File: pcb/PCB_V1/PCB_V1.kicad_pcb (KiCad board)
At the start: 4 copper layers, 100 x 100 mm, 161 parts, among them J201 UART / 3V3 logic, J301 SHT4x / XH 2.50, J302 FLOAT / WAGO 2601, J401 Molex 104031-0811, J501 FAN1 / WAGO 2601, J511 FAN2 / WAGO 2601, J521 PUMP + / switched -, J601 PTC + / switched -, J711 LED1 / large 16S18P panel, J721 LED2 / strip 1, J731 LED3 / strip 2, J901 12 V IN / 25 A design, Q501 AO3400A, Q511 AO3400A, Q521 AO3400A, Q601 NTMFS5C628NLT1G, Q711 100 V N-MOSFET / MPN pending, Q721 100 V N-MOSFET / MPN pending, Q731 100 V N-MOSFET / MPN pending, Q901 P-MOSFET reverse-polarity / M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, SW201 RESET, SW202 BOOT, U101 TPS54202DDCR, U201 ESP32-WROOM-32E-N4, U301 DS3231SN#, U601 UCC27524ADR, U710 LT3756, U720 LT3756, U730 LT3756

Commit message: pcb: repair LED current path and add boost energy storage
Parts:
- added C715: 22u / 25 V X7R / effective >=10u, C_1210_3225Metric, F.Cu at (375.0, 1150.0)
- added C716: 10u / 100 V X7R / effective >=4.7u, C_1210_3225Metric, F.Cu at (175.0, 1200.0)
- added C717: 10u / 100 V X7R / effective >=4.7u, C_1210_3225Metric, F.Cu at (225.0, 1200.0)
- added C725: 22u / 25 V X7R / effective >=10u, C_1210_3225Metric, F.Cu at (225.0, 1250.0)
- added C726: 10u / 100 V X7R / effective >=4.7u, C_1210_3225Metric, F.Cu at (275.0, 1250.0)
- added C727: 10u / 100 V X7R / effective >=4.7u, C_1210_3225Metric, F.Cu at (325.0, 1250.0)
- added C735: 22u / 25 V X7R / effective >=10u, C_1210_3225Metric, F.Cu at (325.0, 1300.0)
- added C736: 10u / 100 V X7R / effective >=4.7u, C_1210_3225Metric, F.Cu at (375.0, 1300.0)
- added C737: 10u / 100 V X7R / effective >=4.7u, C_1210_3225Metric, F.Cu at (175.0, 1350.0)
- C712, C722, C732: value 2.2u / 16 V -> 4.7u / 16 V X7R; footprint C_0603_1608Metric -> C_0805_2012Metric
- R711, R721, R731: value 20k / ~500 kHz preliminary -> 21k / 500 kHz nominal
- R712, R722, R732: value 10k -> 33k / CTRL upper
- R713, R723, R733: value 10k -> 100k / CTRL lower
- R715: value 0.1 / current limit sense -> 0.012 / 1% / >=2W
- R725, R735: value 0.1 / current limit sense -> 0.047 / 1% / >=1W; footprint R_0603_1608Metric -> R_2512_6332Metric
- U710, U720, U730: value LT3756 -> LT3756EMSE-2#PBF
- moved C732 223.6 mm to (175.0, 1300.0)
- moved J711 206.2 mm to (375.0, 1350.0)
- moved L731 206.2 mm to (375.0, 1400.0)
- moved R711 206.2 mm to (375.0, 1450.0)
- moved R716 206.2 mm to (375.0, 1500.0)
- moved R721 206.2 mm to (375.0, 1550.0)
- moved R726 206.2 mm to (375.0, 1600.0)
- moved R731 206.2 mm to (375.0, 1650.0)
- moved R736 206.2 mm to (375.0, 1700.0)
- moved U720 206.2 mm to (375.0, 1750.0)
- moved C722 150.0 mm to (325.0, 1200.0)
- moved C723 150.0 mm to (375.0, 1200.0)
- moved C721 111.8 mm to (275.0, 1200.0)
- moved C724 111.8 mm to (175.0, 1250.0)
- moved D711 111.8 mm to (225.0, 1350.0)
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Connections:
- R716 pad 1: /LEDDrivers/LED1_SENSE_P -> /LEDDrivers/LED1_OUT
- R726 pad 1: /LEDDrivers/LED2_SENSE_P -> /LEDDrivers/LED2_OUT
- R736 pad 1: /LEDDrivers/LED3_SENSE_P -> /LEDDrivers/LED3_OUT
- U710 pad 4: /LEDDrivers/LED1_SENSE_P -> /LEDDrivers/LED1_OUT
- U720 pad 4: /LEDDrivers/LED2_SENSE_P -> /LEDDrivers/LED2_OUT
- U730 pad 4: /LEDDrivers/LED3_SENSE_P -> /LEDDrivers/LED3_OUT

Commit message: pcb: correct power MOSFET pin mapping and reverse input protection
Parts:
- R901: value 100k -> 1M / gate-source
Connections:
- D901 pad 1: +12V_FUSED -> +12V_PROTECTED
- D902 pad 1: +12V_FUSED -> +12V_PROTECTED
- Q711 pad 1: /LEDDrivers/LED1_GATE -> /LEDDrivers/LED1_IS
- Q711 pad 2: /LEDDrivers/LED1_SW -> /LEDDrivers/LED1_IS
- Q711 pad 4: (no net) -> /LEDDrivers/LED1_GATE
- Q711 pad 5: (no net) -> /LEDDrivers/LED1_SW
- Q721 pad 1: /LEDDrivers/LED2_GATE -> /LEDDrivers/LED2_IS
- Q721 pad 2: /LEDDrivers/LED2_SW -> /LEDDrivers/LED2_IS
- Q721 pad 4: (no net) -> /LEDDrivers/LED2_GATE
- Q721 pad 5: (no net) -> /LEDDrivers/LED2_SW
- Q731 pad 1: /LEDDrivers/LED3_GATE -> /LEDDrivers/LED3_IS
- Q731 pad 2: /LEDDrivers/LED3_SW -> /LEDDrivers/LED3_IS
- Q731 pad 4: (no net) -> /LEDDrivers/LED3_GATE
- Q731 pad 5: (no net) -> /LEDDrivers/LED3_SW
- Q901 pad 1: /InputPower/Q901_GATE -> +12V_PROTECTED
- Q901 pad 3: +12V_FUSED -> +12V_PROTECTED
- Q901 pad 4: (no net) -> /InputPower/Q901_GATE
- Q901 pad 5: (no net) -> +12V_FUSED
- R901 pad 1: +12V_FUSED -> +12V_PROTECTED

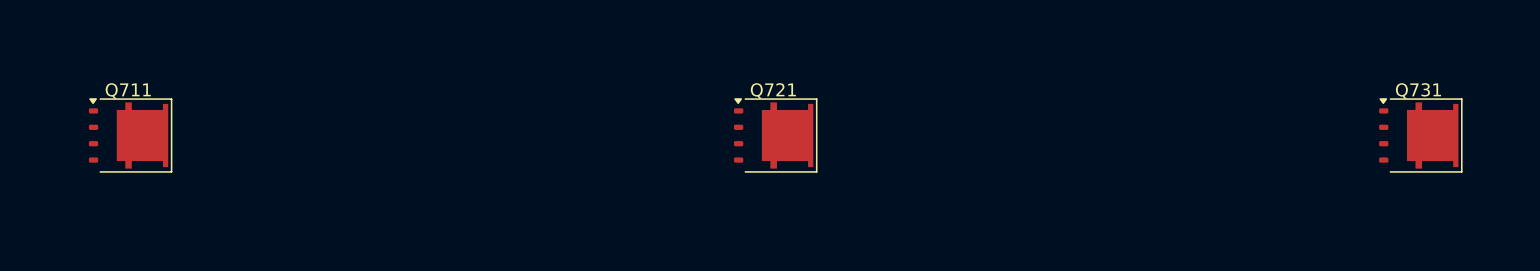
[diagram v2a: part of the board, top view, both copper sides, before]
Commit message: pcb: match LED MOSFET packages and export complete schematic BOM
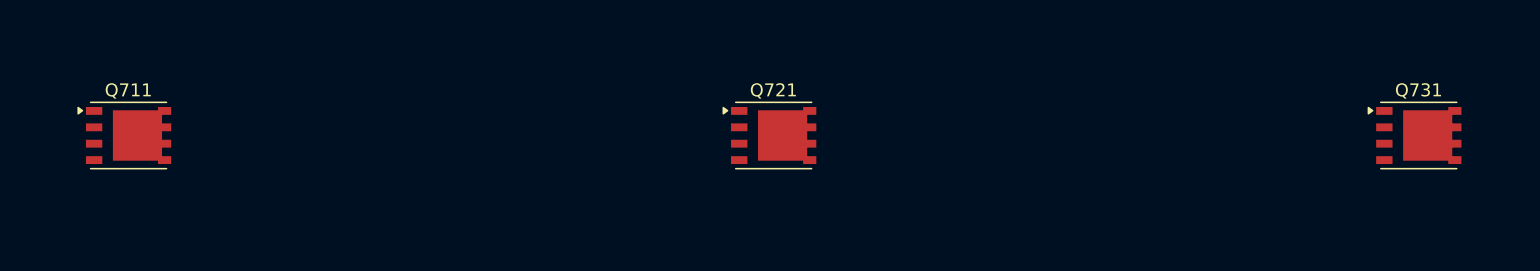
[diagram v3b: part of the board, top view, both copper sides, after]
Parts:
- Q711, Q721, Q731: value 100 V N-MOSFET / MPN pending -> Si7454DDP-T1-GE3; footprint PowerPAK_SO-8L_Single -> Package_SO:PowerPAK_SO-8_Single

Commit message: pcb: replace LT3756 with lower-cost AL8853 LED channels
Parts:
- removed R710, R720, R730: 6.34k / FB divider, R_0603_1608Metric
- removed R719, R729, R739: 249k / FB divider, R_0603_1608Metric
- added C700: 100n 16V, C_0603_1608Metric, F.Cu at (175.0, 1150.0)
- added R701: 47k, R_0603_1608Metric, F.Cu at (375.0, 1450.0)
- added R702: 47k, R_0603_1608Metric, F.Cu at (175.0, 1500.0)
- added R703: 47k, R_0603_1608Metric, F.Cu at (225.0, 1500.0)
- added U700: SN74LVC1G08DBVR, SOT-23-5, F.Cu at (225.0, 1750.0)
- C711, C721, C731: value 100n / 25 V -> 1u 25V X7R; footprint C_0603_1608Metric -> C_0805_2012Metric
- C712, C722, C732: value 4.7u / 16 V X7R -> 100p / comp tune; footprint C_0805_2012Metric -> C_0603_1608Metric
- C713, C723, C733: value 100n soft-start -> 100p / CS tune
- C714, C724, C734: value 2.2n compensation -> 220n / comp tune
- C715, C725, C735: value 22u / 25 V X7R / effective >=10u -> 22u 25V X7R
- C716, C717, C726, C727, C736, C737: value 10u / 100 V X7R / effective >=4.7u -> 10u 100V X7R
- D711, D721, D731: value 100 V Schottky / MPN pending -> 100V 5A / MPN TBD
- J711: value LED1 / large 16S18P panel -> LED +/- (return isolated); footprint TerminalBlock_WAGO_2601-1102_1x02_P3.50mm_Horizontal -> TerminalBlock_Phoenix_MKDS-1,5-2-5.08_1x02_P5.08mm_Horizontal
- J721: value LED2 / strip 1 -> LED +/- (return isolated); footprint TerminalBlock_WAGO_2601-1102_1x02_P3.50mm_Horizontal -> TerminalBlock_Phoenix_MKDS-1,5-2-5.08_1x02_P5.08mm_Horizontal
- J731: value LED3 / strip 2 -> LED +/- (return isolated); footprint TerminalBlock_WAGO_2601-1102_1x02_P3.50mm_Horizontal -> TerminalBlock_Phoenix_MKDS-1,5-2-5.08_1x02_P5.08mm_Horizontal
- L711: value 22uH / Isat >= 10 A -> 47u / Isat>=14A / TBD; footprint L_10.4x10.4_H4.8 -> L_Bourns_SRP1245A
- L721, L731: value 47uH / Isat >= 3 A -> 100u / Isat>=5A / TBD; footprint L_10.4x10.4_H4.8 -> L_Bourns_SRP1245A
- Q711: value Si7454DDP-T1-GE3 -> SiR106ADP-T1-RE3; footprint Package_SO:PowerPAK_SO-8_Single -> PowerPAK_SO-8_Single
- Q721, Q731: footprint Package_SO:PowerPAK_SO-8_Single -> PowerPAK_SO-8_Single
- R711, R721, R731: value 21k / 500 kHz nominal -> 10R
- R712, R722, R732: value 33k / CTRL upper -> 1k / slope tune
- R713, R723, R733: value 100k / CTRL lower -> 100k
- R714, R724, R734: value 10k -> 10k / comp tune
- R715: value 0.012 / 1% / >=2W -> 0.027 1% >=2W
- R716: value 0.091 / 1% -> 0.182 1% >=1W
- R717, R727, R737: value 249k / OVP divider -> 316k 1%
- R718, R728, R738: value 6.34k / OVP divider -> 10k 1%
- R725, R735: value 0.047 / 1% / >=1W -> 0.10 1% >=1W
- R726, R736: value 0.40 / 1% -> 0.80 1% >=0.25W; footprint R_0603_1608Metric -> R_1206_3216Metric
- U710, U720, U730: value LT3756EMSE-2#PBF -> AL8853S-13; footprint MSOP-16-1EP_3x4.039mm_P0.5mm_EP1.651x2.845mm_ThermalVias -> SOIC-8_3.9x4.9mm_P1.27mm
- moved C715 206.2 mm to (175.0, 1200.0)
- moved C723 206.2 mm to (175.0, 1250.0)
- moved C731 206.2 mm to (175.0, 1300.0)
- moved C736 206.2 mm to (175.0, 1350.0)
- moved J711 206.2 mm to (175.0, 1400.0)
- moved L731 206.2 mm to (175.0, 1450.0)
- moved R721 206.2 mm to (175.0, 1600.0)
- moved R726 206.2 mm to (175.0, 1650.0)
- moved R732 206.2 mm to (375.0, 1650.0)
- moved R737 206.2 mm to (375.0, 1700.0)
- moved U730 206.2 mm to (375.0, 1750.0)
- moved R712 150.0 mm to (325.0, 1500.0)
- moved R713 150.0 mm to (375.0, 1500.0)
- moved R717 150.0 mm to (325.0, 1550.0)
- moved R718 150.0 mm to (375.0, 1550.0)
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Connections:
- C712 pad 1: /LEDDrivers/LED1_INTVCC -> /LEDDrivers/LED1_COMP
- C713 pad 1: /LEDDrivers/LED1_SS -> /LEDDrivers/LED1_CS
- C722 pad 1: /LEDDrivers/LED2_INTVCC -> /LEDDrivers/LED2_COMP
- C723 pad 1: /LEDDrivers/LED2_SS -> /LEDDrivers/LED2_CS
- C732 pad 1: /LEDDrivers/LED3_INTVCC -> /LEDDrivers/LED3_COMP
- C733 pad 1: /LEDDrivers/LED3_SS -> /LEDDrivers/LED3_CS
- J711 pad 1: /LEDDrivers/LED1_LEDPLUS -> /LEDDrivers/LED1_OUT
- J711 pad 2: GND -> /LEDDrivers/LED1_RETURN
- J721 pad 1: /LEDDrivers/LED2_LEDPLUS -> /LEDDrivers/LED2_OUT
- J721 pad 2: GND -> /LEDDrivers/LED2_RETURN
- J731 pad 1: /LEDDrivers/LED3_LEDPLUS -> /LEDDrivers/LED3_OUT
- J731 pad 2: GND -> /LEDDrivers/LED3_RETURN
- Q711 pad 1: /LEDDrivers/LED1_IS -> /LEDDrivers/LED1_SOURCE
- Q711 pad 2: /LEDDrivers/LED1_IS -> /LEDDrivers/LED1_SOURCE
- Q711 pad 3: /LEDDrivers/LED1_IS -> /LEDDrivers/LED1_SOURCE
- Q721 pad 1: /LEDDrivers/LED2_IS -> /LEDDrivers/LED2_SOURCE
- Q721 pad 2: /LEDDrivers/LED2_IS -> /LEDDrivers/LED2_SOURCE
- Q721 pad 3: /LEDDrivers/LED2_IS -> /LEDDrivers/LED2_SOURCE
- Q731 pad 1: /LEDDrivers/LED3_IS -> /LEDDrivers/LED3_SOURCE
- Q731 pad 2: /LEDDrivers/LED3_IS -> /LEDDrivers/LED3_SOURCE
- Q731 pad 3: /LEDDrivers/LED3_IS -> /LEDDrivers/LED3_SOURCE
- R711 pad 1: /LEDDrivers/LED1_RT -> /LEDDrivers/LED1_DRV
- R711 pad 2: GND -> /LEDDrivers/LED1_GATE
- R712 pad 1: /LEDDrivers/LED1_VREF -> /LEDDrivers/LED1_SOURCE
- R712 pad 2: /LEDDrivers/LED1_CTRL -> /LEDDrivers/LED1_CS
- R713 pad 1: /LEDDrivers/LED1_CTRL -> /LEDDrivers/LED1_GATE
- R713 pad 2: GND -> /LEDDrivers/LED1_SOURCE
- R715 pad 1: /LEDDrivers/LED1_IS -> /LEDDrivers/LED1_SOURCE
- R716 pad 1: /LEDDrivers/LED1_OUT -> /LEDDrivers/LED1_RETURN
- R716 pad 2: /LEDDrivers/LED1_LEDPLUS -> GND
- R721 pad 1: /LEDDrivers/LED2_RT -> /LEDDrivers/LED2_DRV
- R721 pad 2: GND -> /LEDDrivers/LED2_GATE
- R722 pad 1: /LEDDrivers/LED2_VREF -> /LEDDrivers/LED2_SOURCE
- R722 pad 2: /LEDDrivers/LED2_CTRL -> /LEDDrivers/LED2_CS
- R723 pad 1: /LEDDrivers/LED2_CTRL -> /LEDDrivers/LED2_GATE
- R723 pad 2: GND -> /LEDDrivers/LED2_SOURCE
- R725 pad 1: /LEDDrivers/LED2_IS -> /LEDDrivers/LED2_SOURCE
- R726 pad 1: /LEDDrivers/LED2_OUT -> /LEDDrivers/LED2_RETURN
- R726 pad 2: /LEDDrivers/LED2_LEDPLUS -> GND
- R731 pad 1: /LEDDrivers/LED3_RT -> /LEDDrivers/LED3_DRV
- R731 pad 2: GND -> /LEDDrivers/LED3_GATE
- R732 pad 1: /LEDDrivers/LED3_VREF -> /LEDDrivers/LED3_SOURCE
- R732 pad 2: /LEDDrivers/LED3_CTRL -> /LEDDrivers/LED3_CS
- R733 pad 1: /LEDDrivers/LED3_CTRL -> /LEDDrivers/LED3_GATE
- R733 pad 2: GND -> /LEDDrivers/LED3_SOURCE
- R735 pad 1: /LEDDrivers/LED3_IS -> /LEDDrivers/LED3_SOURCE
- R736 pad 1: /LEDDrivers/LED3_OUT -> /LEDDrivers/LED3_RETURN
- R736 pad 2: /LEDDrivers/LED3_LEDPLUS -> GND
- U710 pad 1: unconnected-(U710-PWMOUT-Pad1) -> +12V_LED
- U710 pad 2: /LEDDrivers/LED1_FB -> /LEDDrivers/LED1_DRV
- U710 pad 3: /LEDDrivers/LED1_LEDPLUS -> GND
- U710 pad 4: /LEDDrivers/LED1_OUT -> /LEDDrivers/LED1_CS
- U710 pad 5: /LEDDrivers/LED1_COMP -> /LEDDrivers/LED1_RETURN
- U710 pad 6: /LEDDrivers/LED1_CTRL -> /LEDDrivers/LED1_COMP
- U710 pad 7: /LEDDrivers/LED1_VREF -> /LEDDrivers/LED1_OVP
- U710 pad 8: LIGHT_PWM -> /LEDDrivers/LED_DIM
- U720 pad 1: unconnected-(U720-PWMOUT-Pad1) -> +12V_LED
- U720 pad 2: /LEDDrivers/LED2_FB -> /LEDDrivers/LED2_DRV
- U720 pad 3: /LEDDrivers/LED2_LEDPLUS -> GND
- U720 pad 4: /LEDDrivers/LED2_OUT -> /LEDDrivers/LED2_CS
- U720 pad 5: /LEDDrivers/LED2_COMP -> /LEDDrivers/LED2_RETURN
- U720 pad 6: /LEDDrivers/LED2_CTRL -> /LEDDrivers/LED2_COMP
- U720 pad 7: /LEDDrivers/LED2_VREF -> /LEDDrivers/LED2_OVP
- U720 pad 8: LIGHT_PWM -> /LEDDrivers/LED_DIM
- U730 pad 1: unconnected-(U730-PWMOUT-Pad1) -> +12V_LED
- U730 pad 2: /LEDDrivers/LED3_FB -> /LEDDrivers/LED3_DRV
- U730 pad 3: /LEDDrivers/LED3_LEDPLUS -> GND
- U730 pad 4: /LEDDrivers/LED3_OUT -> /LEDDrivers/LED3_CS
- U730 pad 5: /LEDDrivers/LED3_COMP -> /LEDDrivers/LED3_RETURN
- U730 pad 6: /LEDDrivers/LED3_CTRL -> /LEDDrivers/LED3_COMP
- U730 pad 7: /LEDDrivers/LED3_VREF -> /LEDDrivers/LED3_OVP
- U730 pad 8: LIGHT_PWM -> /LEDDrivers/LED_DIM

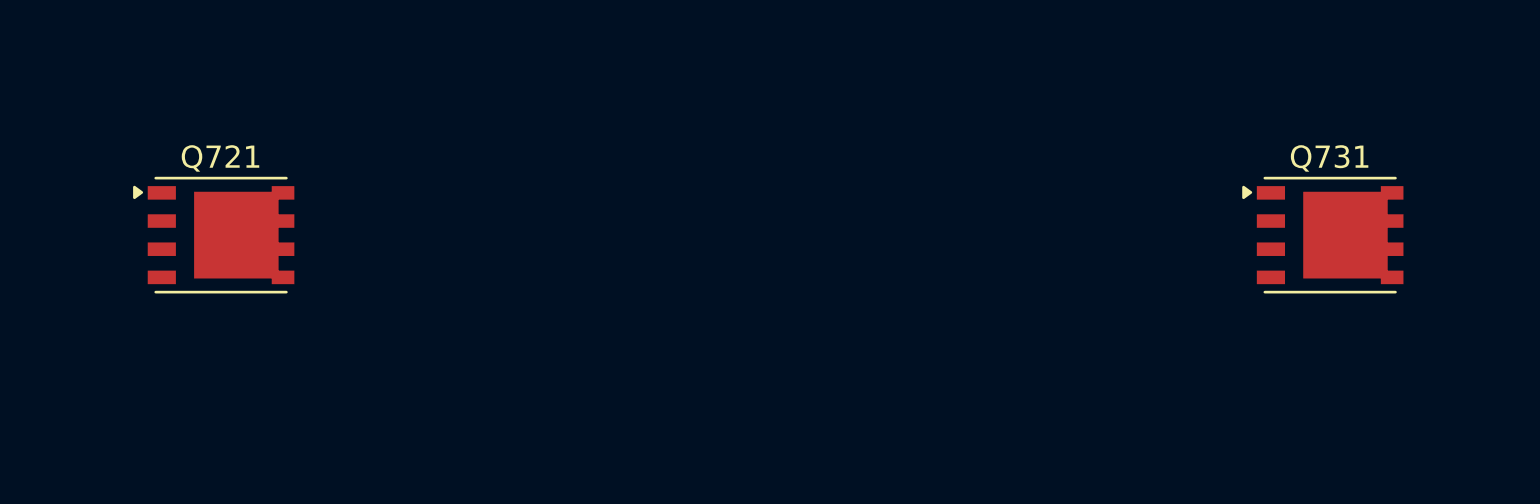
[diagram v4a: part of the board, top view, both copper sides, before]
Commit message: pcb: replace strip LED MOSFETs with DMT10H009LK3 DPAK parts
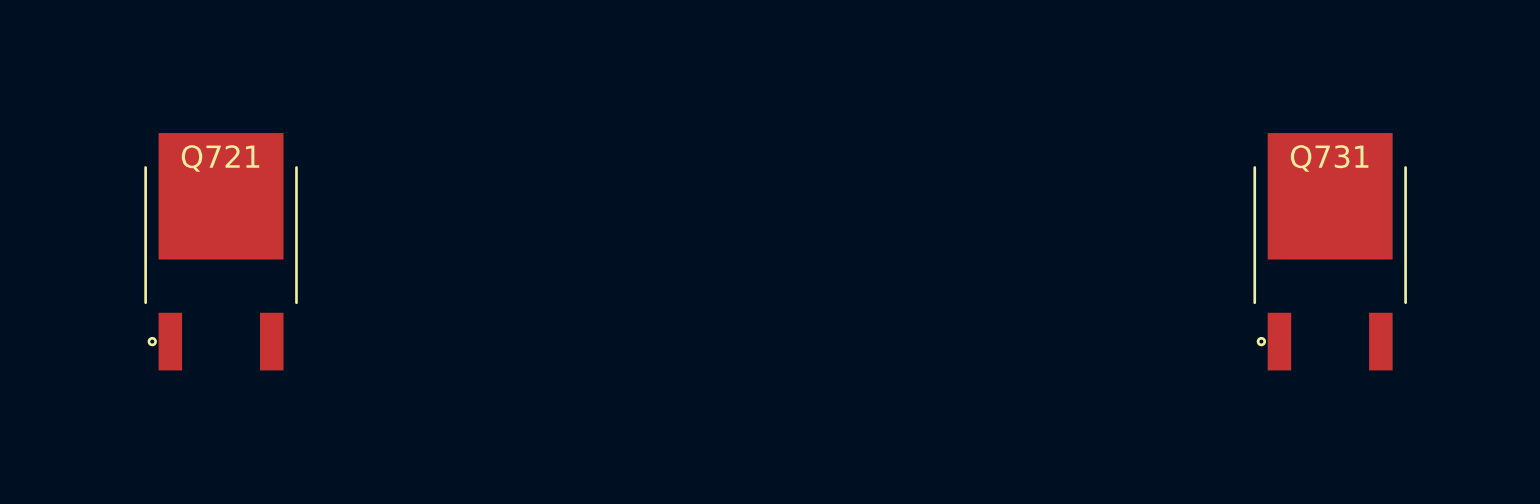
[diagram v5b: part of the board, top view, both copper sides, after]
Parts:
- Q721, Q731: value Si7454DDP-T1-GE3 -> DMT10H009LK3-13; footprint PowerPAK_SO-8_Single -> GrowBox:Diodes_TO252_DMT10H009LK3
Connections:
- Q721 pad 1: /LEDDrivers/LED2_SOURCE -> /LEDDrivers/LED2_GATE
- Q721 pad 2: /LEDDrivers/LED2_SOURCE -> /LEDDrivers/LED2_SW
- Q731 pad 1: /LEDDrivers/LED3_SOURCE -> /LEDDrivers/LED3_GATE
- Q731 pad 2: /LEDDrivers/LED3_SOURCE -> /LEDDrivers/LED3_SW

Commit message: pcb: adopt DS3231MZ RTC and compact TI strip MOSFETs
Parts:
- Q721, Q731: value DMT10H009LK3-13 -> CSD19538Q3A; footprint GrowBox:Diodes_TO252_DMT10H009LK3 -> GrowBox:TI_DNH0008A_CSD19538Q3A
- U301: value DS3231SN# -> DS3231MZ+TRL; footprint SOIC-16W_7.5x10.3mm_P1.27mm -> Package_SO:SOIC-8_3.9x4.9mm_P1.27mm
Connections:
- Q721 pad 1: /LEDDrivers/LED2_GATE -> /LEDDrivers/LED2_SOURCE
- Q721 pad 2: /LEDDrivers/LED2_SW -> /LEDDrivers/LED2_SOURCE
- Q731 pad 1: /LEDDrivers/LED3_GATE -> /LEDDrivers/LED3_SOURCE
- Q731 pad 2: /LEDDrivers/LED3_SW -> /LEDDrivers/LED3_SOURCE
- U301 pad 6: GND -> /MCU / ESP32/Peripherals/RTC_VBAT
- U301 pad 7: GND -> I2C_SDA
- U301 pad 8: GND -> I2C_SCL

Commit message: pcb: select LED power passives and add sizing checks
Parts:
- added C718: 10u 100V X7S, Capacitor_SMD:C_1210_3225Metric, F.Cu at (525.0, 1200.0)
- added C719: 10u 100V X7S, Capacitor_SMD:C_1210_3225Metric, F.Cu at (575.0, 1200.0)
- BT301: footprint BatteryHolder_Keystone_3002_1x2032 -> Battery:BatteryHolder_Keystone_3002_1x2032
- C101, C521, C715, C725, C735, C902: footprint C_1210_3225Metric -> Capacitor_SMD:C_1210_3225Metric
- C102, C103, C106, C202, C203, C301, C302, C303, C402, C601, C700, C712, C713, C714, C722, C723, C724, C732, C733, C734: footprint C_0603_1608Metric -> Capacitor_SMD:C_0603_1608Metric
- C104, C105, C201, C401, C602, C711, C721, C731: footprint C_0805_2012Metric -> Capacitor_SMD:C_0805_2012Metric
- C716, C717, C726, C727, C736, C737: value 10u 100V X7R -> 10u 100V X7S; footprint C_1210_3225Metric -> Capacitor_SMD:C_1210_3225Metric
- C901: footprint CP_Elec_10x10.5 -> Capacitor_SMD:CP_Elec_10x10.5
- D301, D302, D401, D402, D403, D501, D511: footprint SOT-323_SC-70 -> Package_TO_SOT_SMD:SOT-323_SC-70
- D521: footprint D_SMC -> Diode_SMD:D_SMC
- D601, D901: footprint D_SMB -> Diode_SMD:D_SMB
- D711: value 100V 5A / MPN TBD -> STPS5H100B-TR; footprint D_SMC -> Package_TO_SOT_SMD:TO-252-2
- D721, D731: value 100V 5A / MPN TBD -> STPS2H100AFY; footprint D_SMC -> Diode_SMD:D_SOD-128
- D902: footprint D_SOD-323 -> Diode_SMD:D_SOD-323
- F301: footprint Fuse_1206_3216Metric -> Fuse:Fuse_1206_3216Metric
- F901, F902, F903: footprint Fuse_2920_7451Metric -> Fuse:Fuse_2920_7451Metric
- J201: footprint PinHeader_1x06_P2.54mm_Vertical -> Connector_PinHeader_2.54mm:PinHeader_1x06_P2.54mm_Vertical
- J301: footprint JST_XH_B4B-XH-A_1x04_P2.50mm_Vertical -> Connector_JST:JST_XH_B4B-XH-A_1x04_P2.50mm_Vertical
- J302, J521, J601: footprint TerminalBlock_WAGO_2601-1102_1x02_P3.50mm_Horizontal -> TerminalBlock_WAGO:TerminalBlock_WAGO_2601-1102_1x02_P3.50mm_Horizontal
- J401: footprint microSD_HC_Molex_104031-0811 -> Connector_Card:microSD_HC_Molex_104031-0811
- J501, J511: footprint TerminalBlock_WAGO_2601-1104_1x04_P3.50mm_Horizontal -> TerminalBlock_WAGO:TerminalBlock_WAGO_2601-1104_1x04_P3.50mm_Horizontal
- J711, J721, J731, J901: footprint TerminalBlock_Phoenix_MKDS-1,5-2-5.08_1x02_P5.08mm_Horizontal -> TerminalBlock_Phoenix:TerminalBlock_Phoenix_MKDS-1,5-2-5.08_1x02_P5.08mm_Horizontal
- L101: footprint L_Coilcraft_XAL7050-XXX -> Inductor_SMD:L_Coilcraft_XAL7050-XXX
- L711: value 47u / Isat>=14A / TBD -> 47u SRP1770TA-470M; footprint L_Bourns_SRP1245A -> Inductor_SMD:L_Bourns_SRP1770TA_16.9x16.9mm
- L721, L731: value 100u / Isat>=5A / TBD -> 47u SRP1265A-470M; footprint L_Bourns_SRP1245A -> GrowBox:L_Bourns_SRP1265A
- Q501, Q511, Q521: footprint SOT-23 -> Package_TO_SOT_SMD:SOT-23
- Q601: footprint ONSemi_SO-8FL_488AA -> Package_SO:ONSemi_SO-8FL_488AA
- Q711: footprint PowerPAK_SO-8_Single -> Package_SO:PowerPAK_SO-8_Single
- Q901: footprint PowerPAK_SO-8L_Single -> Package_SO:PowerPAK_SO-8L_Single
- R101, R102, R201, R202, R203, R204, R205, R206, R207, R208, R209, R210, R211, R212, R301, R302, R303, R304, R305, R306, R401, R402, R403, R404, R405, R406, R407, R408, R410, R501, R502, R503, R511, R512, R513, R521, R522, R601, R602, R701, R702, R703, R711, R713, R714, R717, R718, R721, R723, R724, R727, R728, R731, R733, R734, R737, R738, R901, R902: footprint R_0603_1608Metric -> Resistor_SMD:R_0603_1608Metric
- R409: footprint R_0805_2012Metric -> Resistor_SMD:R_0805_2012Metric
- R712: value 1k / slope tune -> 1k 1% / slope tune; footprint R_0603_1608Metric -> Resistor_SMD:R_0603_1608Metric
- R715, R716: footprint R_2512_6332Metric -> Resistor_SMD:R_2512_6332Metric
- R722, R732: value 1k / slope tune -> 2.7k 1% / slope tune; footprint R_0603_1608Metric -> Resistor_SMD:R_0603_1608Metric
- R725, R735: value 0.10 1% >=1W -> 0.047 1% >=1W; footprint R_2512_6332Metric -> Resistor_SMD:R_2512_6332Metric
- R726, R736: footprint R_1206_3216Metric -> Resistor_SMD:R_1206_3216Metric
- SW201, SW202: footprint SW_SPST_TL3342 -> Button_Switch_SMD:SW_SPST_TL3342
- TP101, TP102, TP103, TP901, TP902, TP903: footprint TestPoint_Pad_D2.0mm -> TestPoint:TestPoint_Pad_D2.0mm
- U101: footprint SOT-23-6 -> Package_TO_SOT_SMD:SOT-23-6
- U201: footprint ESP32-WROOM-32E -> RF_Module:ESP32-WROOM-32E
- U601, U710, U720, U730: footprint SOIC-8_3.9x4.9mm_P1.27mm -> Package_SO:SOIC-8_3.9x4.9mm_P1.27mm
- U700: footprint SOT-23-5 -> Package_TO_SOT_SMD:SOT-23-5
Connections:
- D711 pad 1: /LEDDrivers/LED1_OUT -> unconnected-(D711-NC-Pad1)
- D711 pad 2: /LEDDrivers/LED1_SW -> /LEDDrivers/LED1_OUT

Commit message: pcb: select ideal-diode input protection and regulate heater gate supply
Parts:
- removed D902: 12 V gate clamp / MPN pending, Diode_SMD:D_SOD-323
- removed R901: 1M / gate-source, Resistor_SMD:R_0603_1608Metric
- removed R902: 100k, Resistor_SMD:R_0603_1608Metric
- added C603: 2.2u / 50V X7R, Capacitor_SMD:C_0805_2012Metric, F.Cu at (575.0, 1700.0)
- added C604: 10u / 16V X7R, Capacitor_SMD:C_0805_2012Metric, F.Cu at (625.0, 1700.0)
- added C903: 100n / 50V X7R, Capacitor_SMD:C_0805_2012Metric, F.Cu at (575.0, 1600.0)
- added C904: 220n / 50V X7R, Capacitor_SMD:C_0805_2012Metric, F.Cu at (625.0, 1600.0)
- added R903: 0 / gate link, Resistor_SMD:R_0603_1608Metric, F.Cu at (675.0, 1600.0)
- added U602: TPS70950DBVR, Package_TO_SOT_SMD:SOT-23-5, F.Cu at (525.0, 1700.0)
- added U901: LM74700QDBVRQ1, Package_TO_SOT_SMD:SOT-23-6, F.Cu at (525.0, 1600.0)
- C602: value 1u / 25V -> 2.2u / 25V X7R
- C901: value 220u / 25 V low ESR -> 220u / 35V low ESR
- C902: value 1u / 25 V -> 1u / 50V X7R
- D901: value SMBJ18A-E3/52 -> SMBJ14CA-E3/52
- F902: value 20 A loads branch / verify -> 20 A loads / verify
- F903: value 10 A LED branch / verify -> 10 A LED / verify
- Q901: value P-MOSFET reverse-polarity / MPN pending -> NTMFS5C628NLT1G; footprint Package_SO:PowerPAK_SO-8L_Single -> Package_SO:ONSemi_SO-8FL_488AA
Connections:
- C601 pad 1: +12V_LOADS -> +5V_GATE
- C602 pad 1: +12V_LOADS -> +5V_GATE
- D901 pad 1: +12V_PROTECTED -> +12V_FUSED
- Q901 pad 1: +12V_PROTECTED -> +12V_FUSED
- Q901 pad 2: +12V_PROTECTED -> +12V_FUSED
- Q901 pad 3: +12V_PROTECTED -> +12V_FUSED
- Q901 pad 4: /InputPower/Q901_GATE -> /InputPower/REV_GATE
- Q901 pad 5: +12V_FUSED -> +12V_PROTECTED
- U601 pad 6: +12V_LOADS -> +5V_GATE
